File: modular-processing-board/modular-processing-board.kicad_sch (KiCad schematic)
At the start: 7 parts

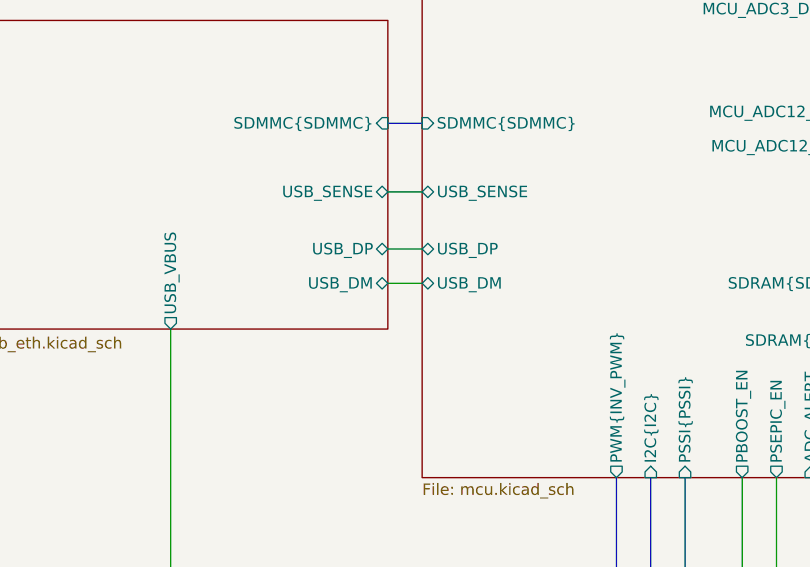
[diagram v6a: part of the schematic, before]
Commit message: replaced sdmmc connector, added smmc trace, added u.fl. connectors
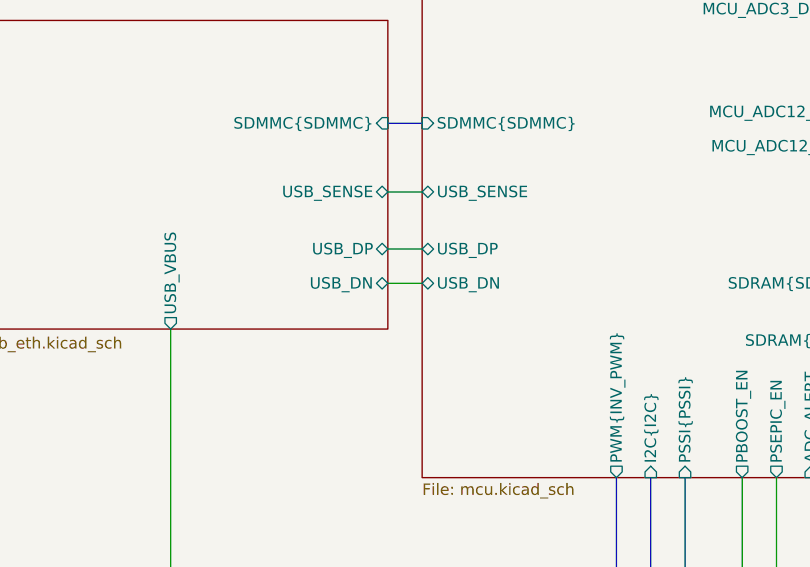
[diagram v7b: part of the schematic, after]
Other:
- sheet mcu ports: added USB_DN; removed USB_DM
- sheet usb ports: added USB_DN; removed USB_DM
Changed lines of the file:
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@@
 			)
 		)
-		(pin "USB_DM" bidirectional
+		(pin "USB_DN" bidirectional
 			(at 93.98 92.71 180)
 			(effects
@@
 			)
 		)
-		(pin "USB_DM" bidirectional
+		(pin "USB_DN" bidirectional
 			(at 90.17 92.71 0)
 			(effects

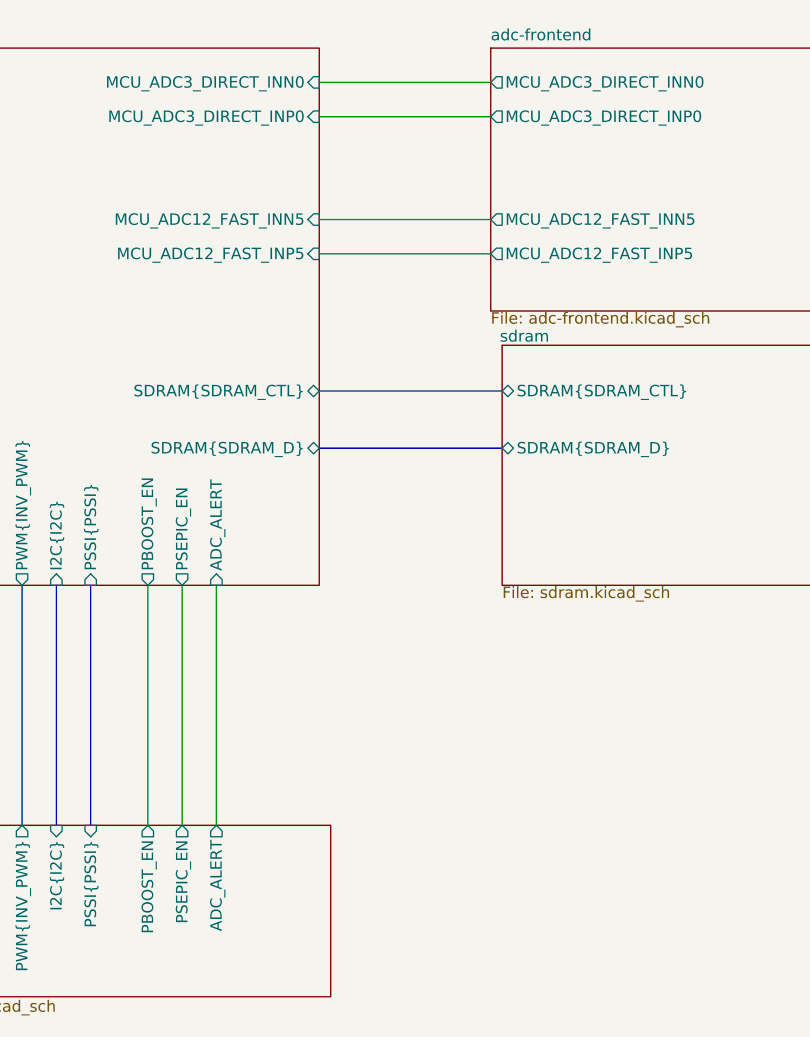
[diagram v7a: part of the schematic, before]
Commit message: reconnected vref
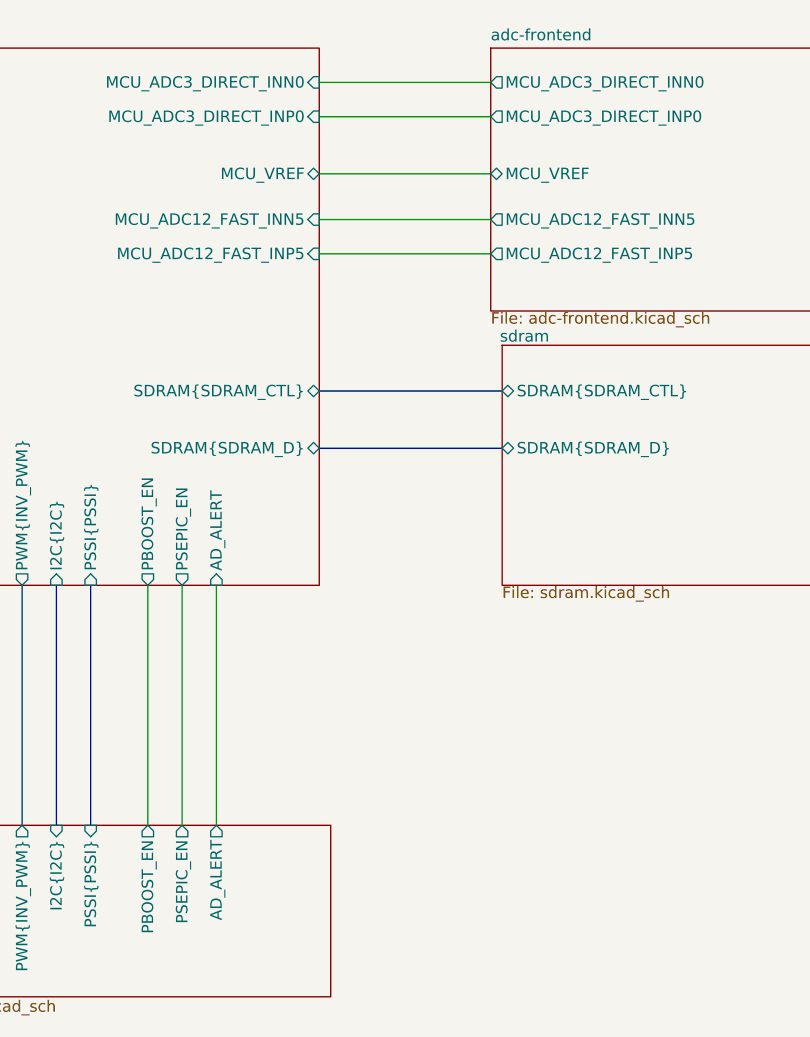
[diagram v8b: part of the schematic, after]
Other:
- sheet adc-frontend ports: added MCU_VREF; removed none
- sheet connectors ports: added AD_ALERT; removed ADC_ALERT
- sheet mcu ports: added AD_ALERT, MCU_VREF; removed ADC_ALERT
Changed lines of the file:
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@@
+	(wire
+		(pts
+			(xy 148.59 68.58) (xy 167.64 68.58)
+		)
+		(stroke
+			(width 0)
+			(type default)
+		)
+	)
 	(wire
 		(pts
@@
 			)
 		)
-		(pin "ADC_ALERT" input
+		(pin "AD_ALERT" input
 			(at 137.16 114.3 270)
 			(effects
@@
 				)
 				(justify left)
+			)
+		)
+		(pin "MCU_VREF" bidirectional
+			(at 148.59 68.58 0)
+			(effects
+				(font
+					(size 1.27 1.27)
+				)
+				(justify right)
 			)
 		)
@@
 			)
 		)
-		(pin "ADC_ALERT" output
+		(pin "AD_ALERT" output
 			(at 137.16 140.97 90)
 			(effects
@@
 			(effects
 				(font
+					(size 1.27 1.27)
+				)
+				(justify left)
+			)
+		)
+		(pin "MCU_VREF" bidirectional
+			(at 167.64 68.58 180)
+			(effects
+				(font
